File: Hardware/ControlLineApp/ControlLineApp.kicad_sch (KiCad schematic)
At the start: 10 parts, among them J2 Conn_02x09

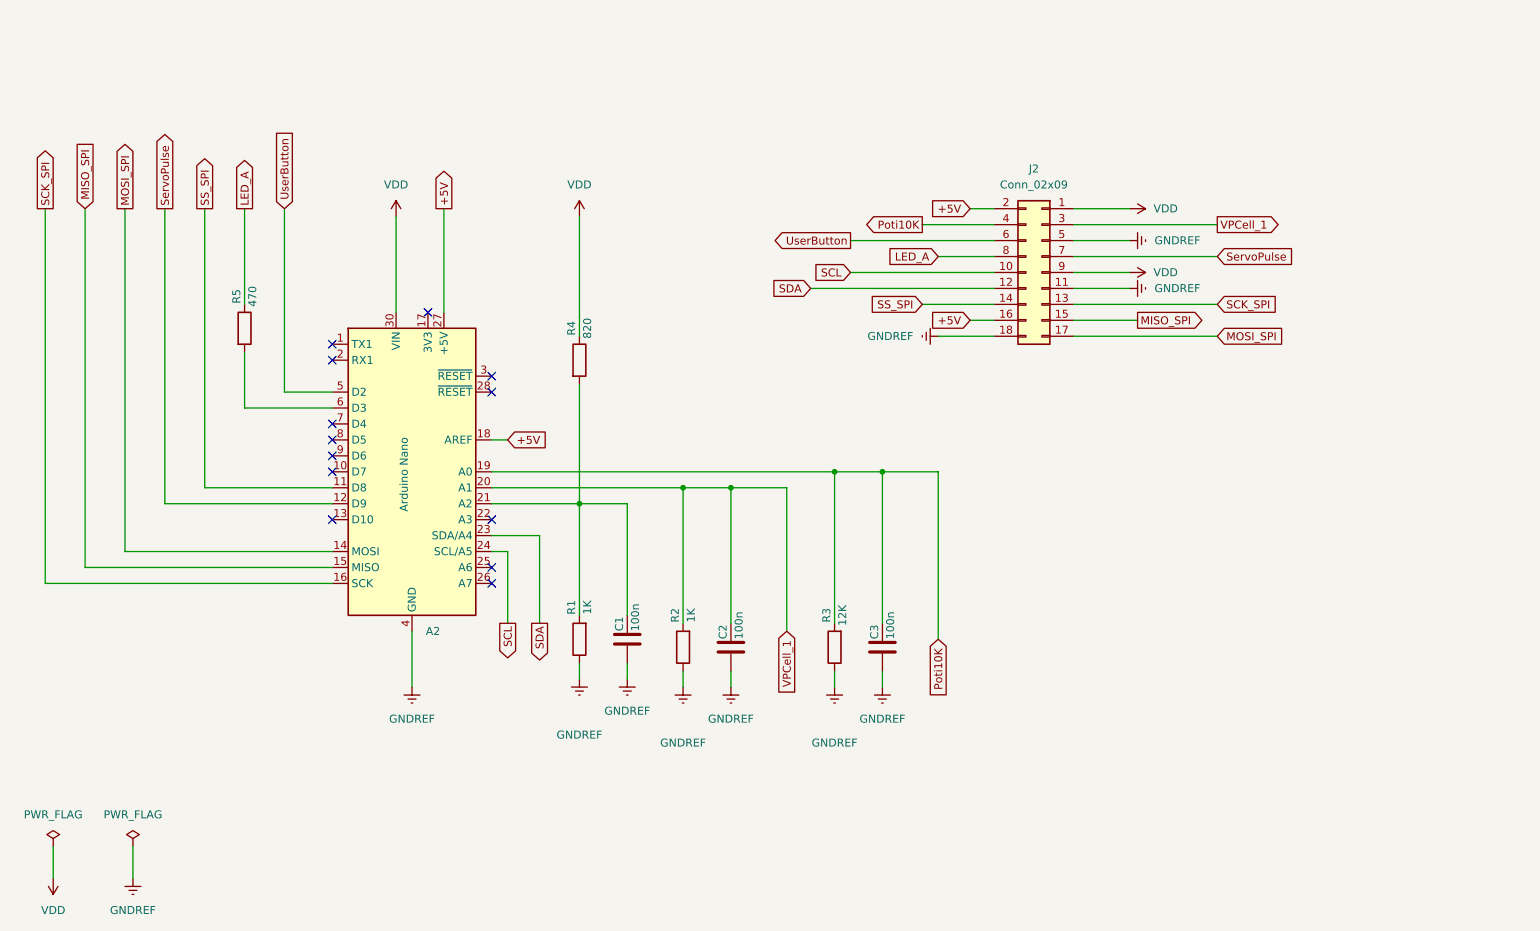
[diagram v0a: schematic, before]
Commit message: App extended with additional functions like retractable landing gear
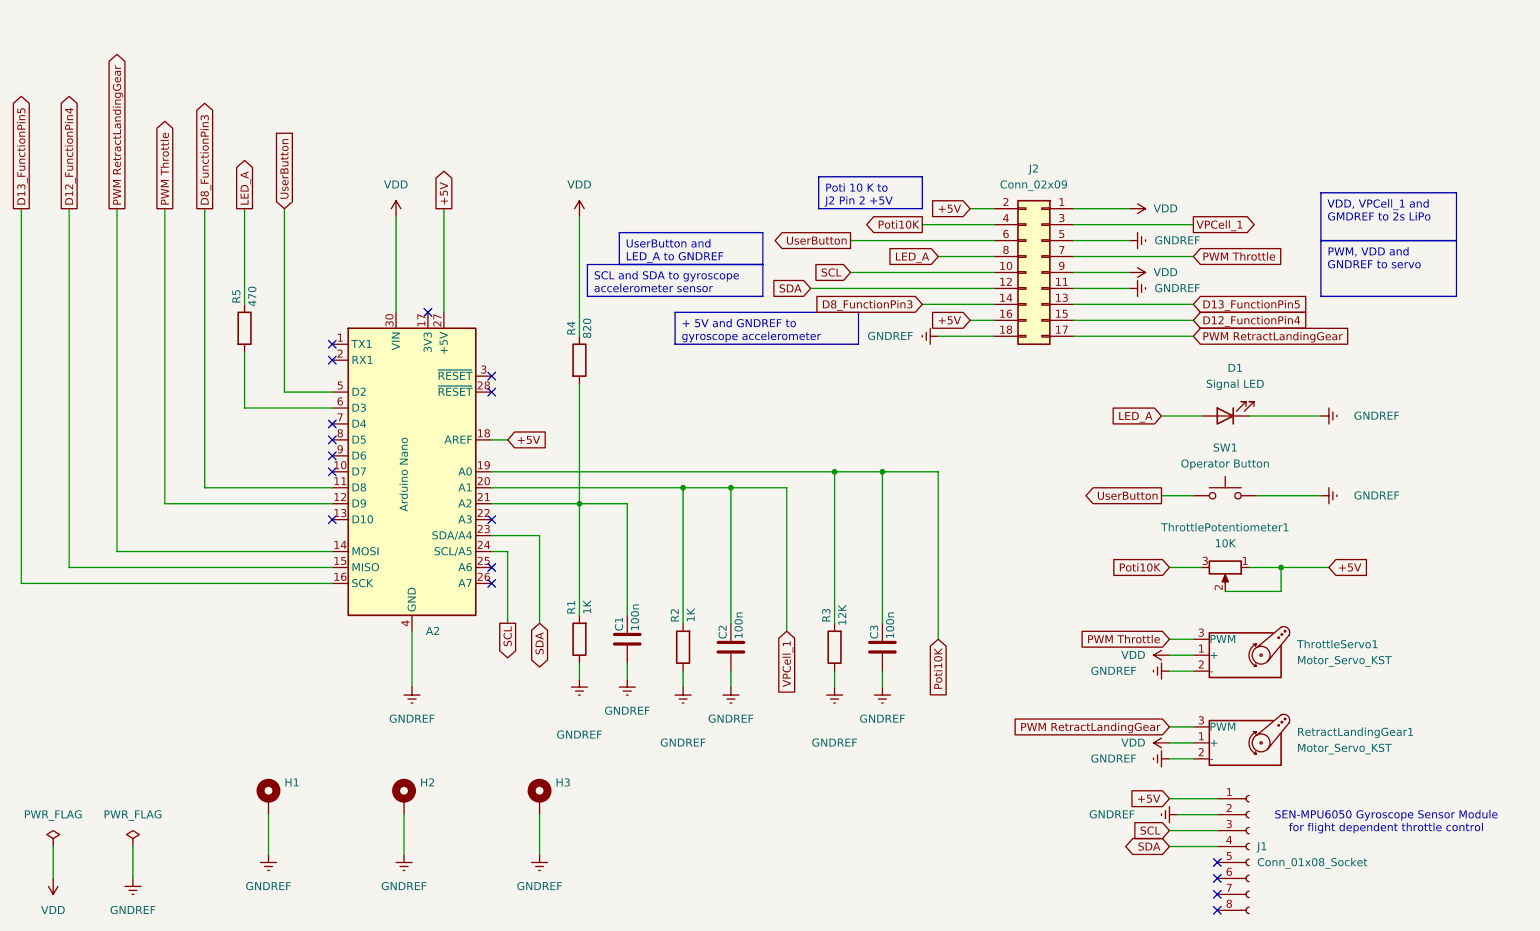
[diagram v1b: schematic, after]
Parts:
- added D1: Signal LED, symbol Device:LED
- added H1, H2, H3: MountingHole_Pad, MountingHole:MountingHole_2.2mm_M2_DIN965_Pad, symbol Mechanical:MountingHole_Pad
- added J1: Conn_01x08_Socket, symbol Connector:Conn_01x08_Socket
- added RetractLandingGear1, ThrottleServo1: Motor_Servo_KST, symbol Motor:Motor_Servo_AirTronics
- added SW1: Operator Button, symbol Switch:SW_Push
- added ThrottlePotentiometer1: 10K, symbol Device:R_Potentiometer
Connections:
- net +5V: now also J1.1 (Pin_1), ThrottlePotentiometer1.1, ThrottlePotentiometer1.2
- net GNDREF: now also D1.1 (K), H1.1, H2.1, H3.1, J1.2 (Pin_2), RetractLandingGear1.2 (-), SW1.2, ThrottleServo1.2 (-)
- net LED_A: now also D1.2 (A)
- net Poti10K: now also ThrottlePotentiometer1.3
- net SCL: now also J1.3 (Pin_3)
- net SDA: now also J1.4 (Pin_4)
- net UserButton: now also SW1.1
- net VDD: now also RetractLandingGear1.1 (+), ThrottleServo1.1 (+)
- net MISO_SPI renamed D12_FunctionPin4
- net MOSI_SPI renamed PWM RetractLandingGear
- net PWM RetractLandingGear: now also RetractLandingGear1.3 (PWM)
- net SCK_SPI renamed D13_FunctionPin5
- net SS_SPI renamed D8_FunctionPin3
- net ServoPulse renamed PWM Throttle
- net PWM Throttle: now also ThrottleServo1.3 (PWM)
- no-connect marks 13 -> 17
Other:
- note added: "SEN-MPU6050 Gyroscope Sensor Module for flight dependent throttle control"
